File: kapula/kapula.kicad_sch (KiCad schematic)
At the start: 153 parts, among them J1 Conn_02x10_Odd_Even, J12 U.FL, J13 U.FL, J4 Conn_ARM_JTAG_SWD_10, J5 U.FL, J9 U.FL, Q1 AO3401A, Q1 BSS84, Q2 AO3401A, Q3 AO3400A, Q5 AO3400A, Q6 AO3400A, T1 BW21S7511A01TF, T2 BW21S7511A01TF, T3 BW21S7511A01TF, T4 BW21S7511A01TF, U1 XC6206P332MR, U2 TP4054, U3 DW01+G, U5 EFR32FG14P233F256GM48-B, U6 XA213-G4J, X1 DSB221SDN, Y1 32768 Hz

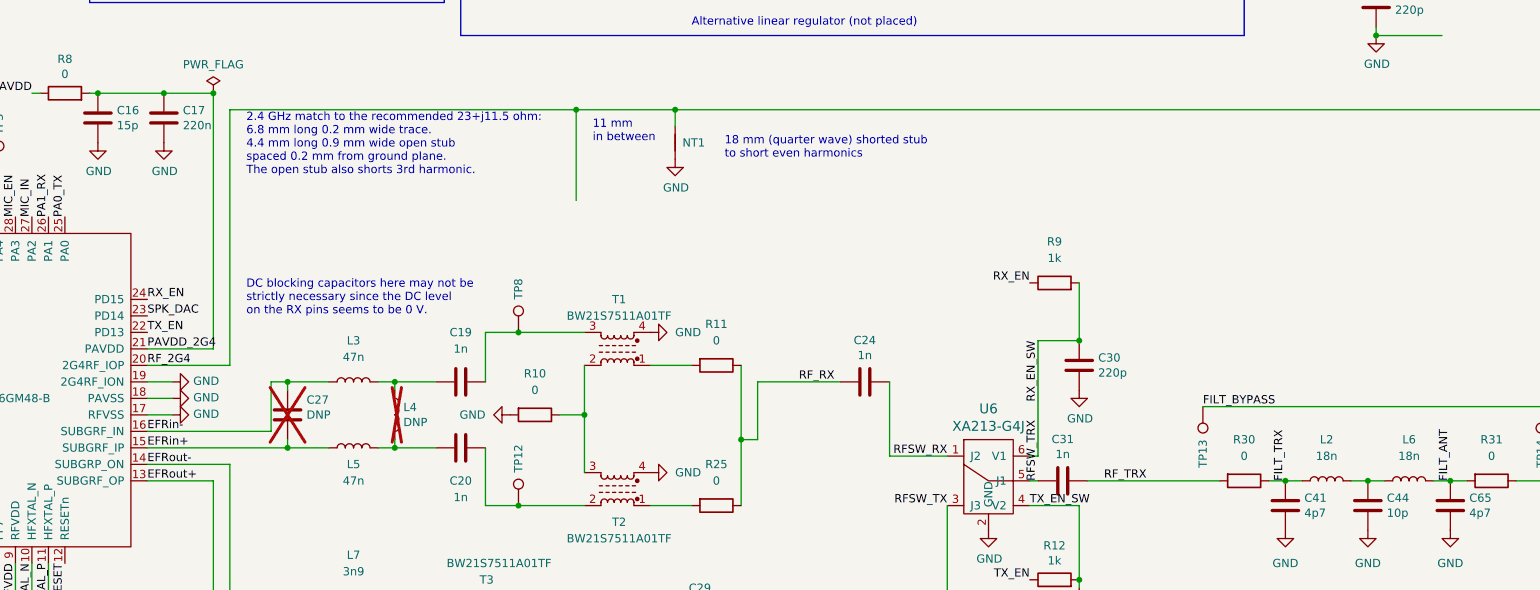
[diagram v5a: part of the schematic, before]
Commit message: PCB: Layout more RF circuits
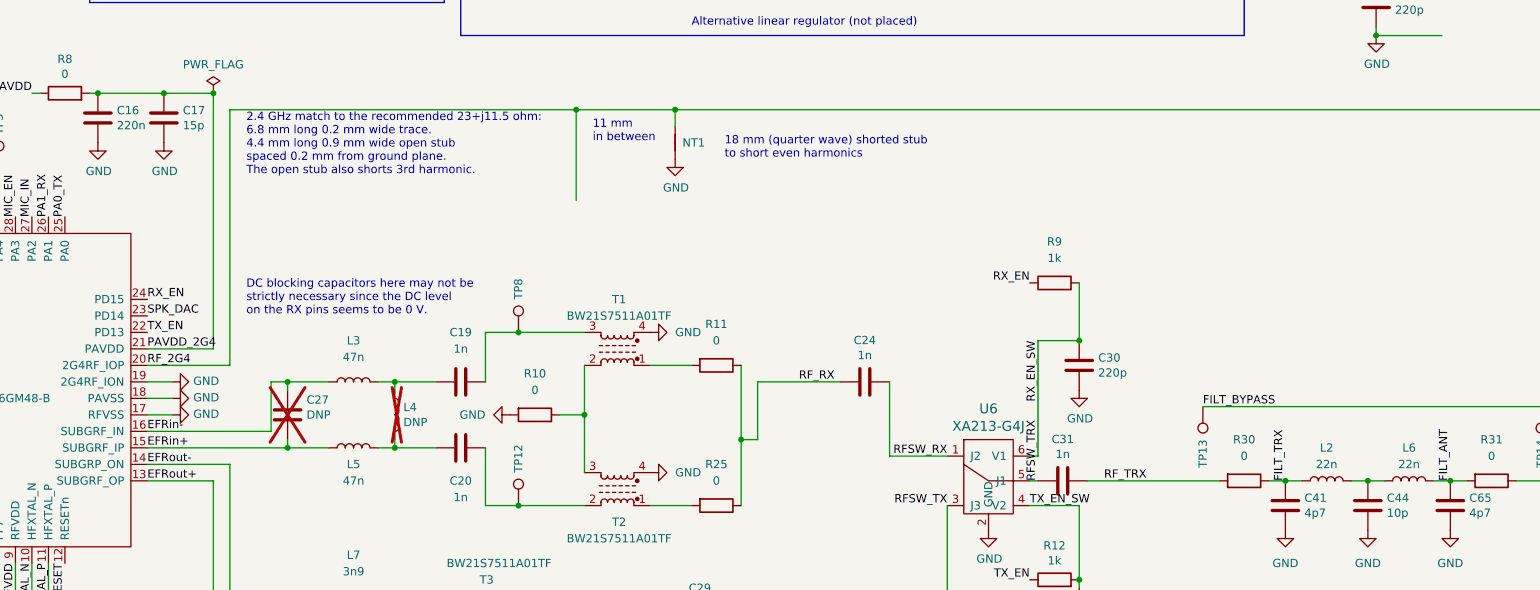
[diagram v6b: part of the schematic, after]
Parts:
- C16: value 15p -> 220n; LCSC C1548 -> C16772
- C17: value 220n -> 15p; LCSC C16772 -> C1548
- C41, C65: LCSC (none) -> C1569
- C44: LCSC (none) -> C32949
- L2, L6: value 18n -> 22n; footprint Inductor_SMD:L_0603_1608Metric_Pad1.05x0.95mm_HandSolder -> kapula:L_0402_to_0603_HandSolder; LCSC (none) -> C12099
- R38, R8: footprint kapula:R_0402_to_0603_HandSolder -> Resistor_SMD:R_0402_1005Metric
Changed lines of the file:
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@@
       (effects (font (size 1.27 1.27)) (justify left))
     )
-    (property "Value" "15p" (at 159.131 87.503 0)
+    (property "Value" "220n" (at 159.131 87.503 0)
       (effects (font (size 1.27 1.27)) (justify left))
     )
@@
       (effects (font (size 1.27 1.27)) hide)
     )
-    (property "LCSC" "C1548" (at 156.21 86.36 0)
+    (property "LCSC" "C16772" (at 156.21 86.36 0)
       (effects (font (size 1.27 1.27)) hide)
     )
@@
       (effects (font (size 1.27 1.27)) (justify left))
     )
-    (property "Value" "220n" (at 169.291 87.503 0)
+    (property "Value" "15p" (at 169.291 87.503 0)
       (effects (font (size 1.27 1.27)) (justify left))
     )
@@
       (effects (font (size 1.27 1.27)) hide)
     )
-    (property "LCSC" "C16772" (at 166.37 86.36 0)
+    (property "LCSC" "C1548" (at 166.37 86.36 0)
       (effects (font (size 1.27 1.27)) hide)
     )
@@
       (effects (font (size 1.27 1.27)))
     )
-    (property "Footprint" "kapula:R_0402_to_0603_HandSolder" (at 151.13 84.328 90)
+    (property "Footprint" "Resistor_SMD:R_0402_1005Metric" (at 151.13 84.328 90)
       (effects (font (size 1.27 1.27)) hide)
     )
@@
       (effects (font (size 1.27 1.27)))
     )
-    (property "Footprint" "kapula:R_0402_to_0603_HandSolder" (at 193.04 191.008 90)
+    (property "Footprint" "Resistor_SMD:R_0402_1005Metric" (at 193.04 191.008 90)
       (effects (font (size 1.27 1.27)) hide)
     )
@@
       (effects (font (size 1.27 1.27)) hide)
     )
-    (property "LCSC" "" (at 351.79 146.05 0)
+    (property "LCSC" "C32949" (at 351.79 146.05 0)
       (effects (font (size 1.27 1.27)) hide)
     )
@@
   (symbol (lib_id "Device:L") (at 358.14 142.24 90) (unit 1)
     (in_bom yes) (on_board yes) (dnp no) (fields_autoplaced)
-    (property "Reference" "L6" (at 358.14 135.89 90)
+    (property "Reference" "L6" (at 358.14 137.16 90)
       (effects (font (size 1.27 1.27)))
     )
-    (property "Value" "18n" (at 358.14 138.43 90)
+    (property "Value" "22n" (at 358.14 139.7 90)
       (effects (font (size 1.27 1.27)))
     )
-    (property "Footprint" "Inductor_SMD:L_0603_1608Metric_Pad1.05x0.95mm_HandSolder" (at 358.14 142.24 0)
+    (property "Footprint" "kapula:L_0402_to_0603_HandSolder" (at 358.14 142.24 0)
       (effects (font (size 1.27 1.27)) hide)
     )
@@
       (effects (font (size 1.27 1.27)) hide)
     )
-    (property "LCSC" "" (at 358.14 142.24 0)
+    (property "LCSC" "C12099" (at 358.14 142.24 0)
       (effects (font (size 1.27 1.27)) hide)
     )
@@
       (effects (font (size 1.27 1.27)) hide)
     )
-    (property "LCSC" "" (at 364.49 146.05 0)
+    (property "LCSC" "C1569" (at 364.49 146.05 0)
       (effects (font (size 1.27 1.27)) hide)
     )
@@
   (symbol (lib_id "Device:L") (at 345.44 142.24 90) (unit 1)
     (in_bom yes) (on_board yes) (dnp no) (fields_autoplaced)
-    (property "Reference" "L2" (at 345.44 135.89 90)
+    (property "Reference" "L2" (at 345.44 137.16 90)
       (effects (font (size 1.27 1.27)))
     )
-    (property "Value" "18n" (at 345.44 138.43 90)
+    (property "Value" "22n" (at 345.44 139.7 90)
       (effects (font (size 1.27 1.27)))
     )
-    (property "Footprint" "Inductor_SMD:L_0603_1608Metric_Pad1.05x0.95mm_HandSolder" (at 345.44 142.24 0)
+    (property "Footprint" "kapula:L_0402_to_0603_HandSolder" (at 345.44 142.24 0)
       (effects (font (size 1.27 1.27)) hide)
     )
@@
       (effects (font (size 1.27 1.27)) hide)
     )
-    (property "LCSC" "" (at 345.44 142.24 0)
+    (property "LCSC" "C12099" (at 345.44 142.24 0)
       (effects (font (size 1.27 1.27)) hide)
     )
@@
       (effects (font (size 1.27 1.27)) hide)
     )
-    (property "LCSC" "" (at 339.09 146.05 0)
+    (property "LCSC" "C1569" (at 339.09 146.05 0)
       (effects (font (size 1.27 1.27)) hide)
     )

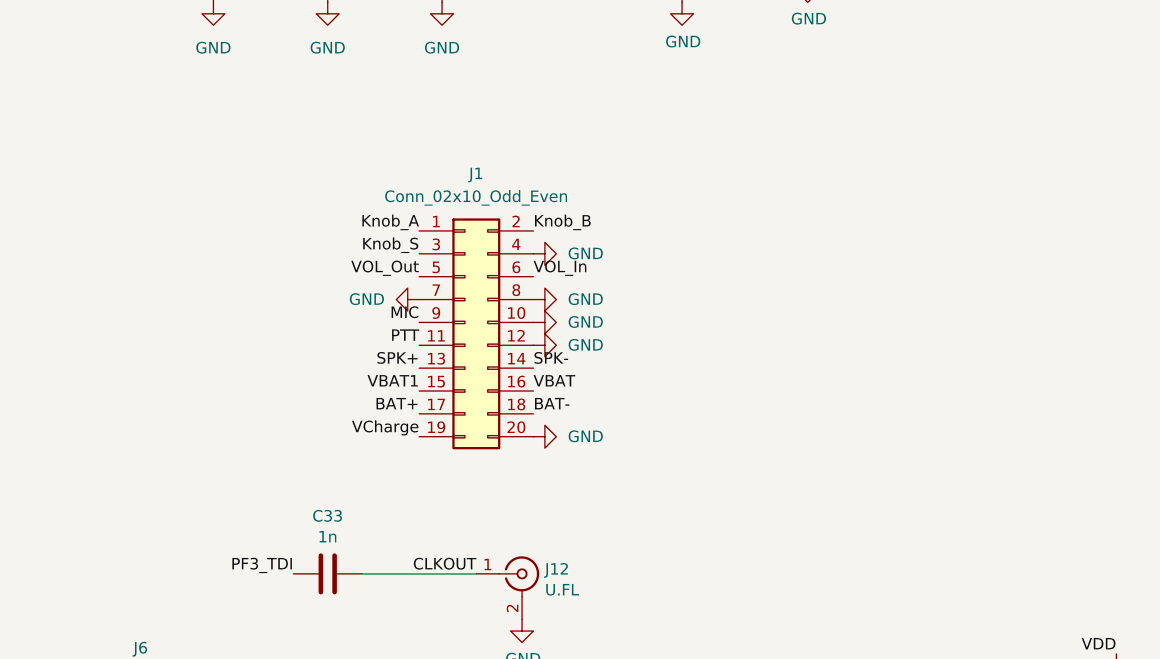
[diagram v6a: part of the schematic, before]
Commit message: PCB: Move components to make space for expansion header
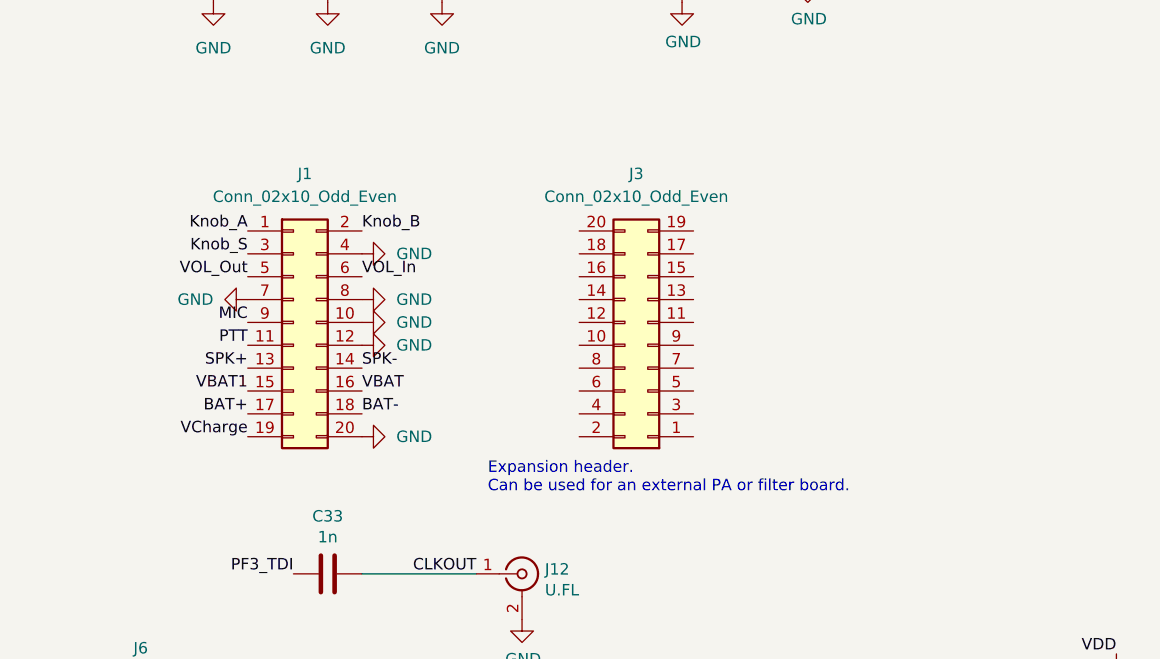
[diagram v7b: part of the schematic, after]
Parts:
- added J3: Conn_02x10_Odd_Even, Connector_PinHeader_2.54mm:PinHeader_2x10_P2.54mm_Vertical, symbol Connector_Generic:Conn_02x10_Odd_Even
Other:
- note added: "Expansion header. Can be used for an external PA or filter board."
- moved on the sheet: J1

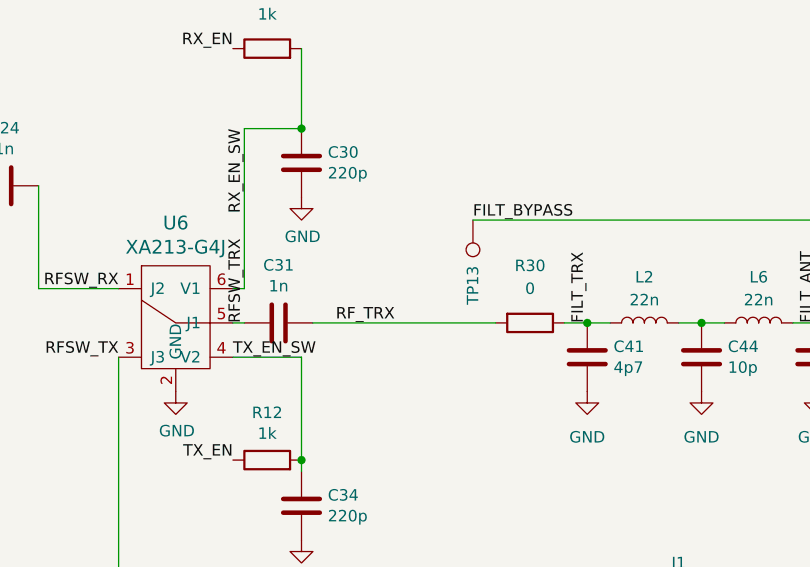
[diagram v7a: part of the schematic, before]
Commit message: PCB: Organize lowpass components to fit them on board again
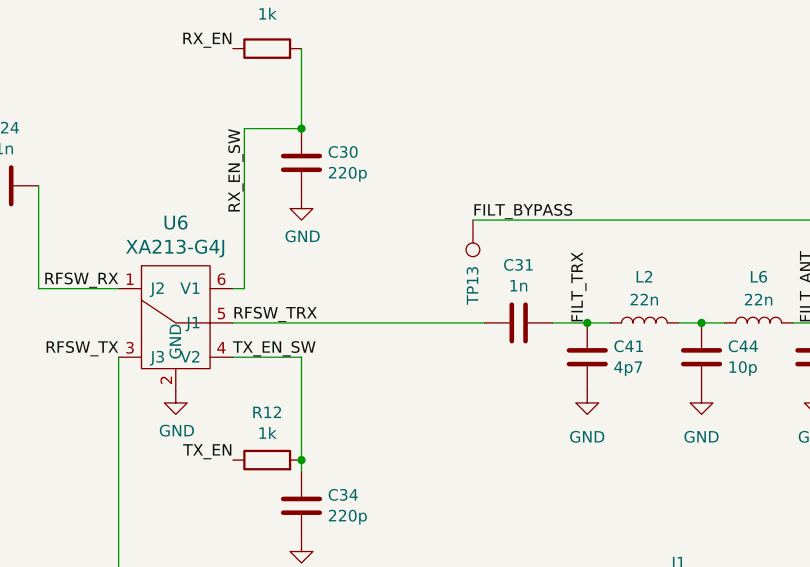
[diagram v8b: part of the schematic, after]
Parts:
- removed R30: 0, kapula:R_0402_to_0603_HandSolder, symbol Device:R
- C31: footprint Capacitor_SMD:C_0402_1005Metric -> kapula:C_0402_to_0603_HandSolder
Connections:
- net RF_TRX is gone; now on net FILT_TRX: C31.1
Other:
- moved on the sheet: C31
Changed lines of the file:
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@@
     (stroke (width 0) (type default))
   )
+  (wire (pts (xy 299.72 142.24) (xy 327.66 142.24))
+    (stroke (width 0) (type default))
+  )
   (wire (pts (xy 307.34 146.05) (xy 299.72 146.05))
     (stroke (width 0) (type default))
@@
     (stroke (width 0) (type default))
   )
-  (wire (pts (xy 308.61 142.24) (xy 328.93 142.24))
-    (stroke (width 0) (type default))
-  )
   (wire (pts (xy 148.59 165.1) (xy 148.59 154.94))
     (stroke (width 0) (type default))
@@
     (stroke (width 0) (type default))
   )
-  (wire (pts (xy 300.99 142.24) (xy 299.72 142.24))
-    (stroke (width 0) (type default))
-  )
-  (wire (pts (xy 336.55 142.24) (xy 339.09 142.24))
+  (wire (pts (xy 335.28 142.24) (xy 339.09 142.24))
     (stroke (width 0) (type default))
   )
@@
     (effects (font (size 1.27 1.27)) (justify right bottom))
   )
-  (label "RFSW_TRX" (at 300.99 142.24 90) (fields_autoplaced)
+  (label "RFSW_TRX" (at 299.72 142.24 0) (fields_autoplaced)
     (effects (font (size 1.27 1.27)) (justify left bottom))
   )
@@
     (effects (font (size 1.27 1.27)) (justify left bottom))
   )
-  (label "RF_TRX" (at 311.15 142.24 0) (fields_autoplaced)
-    (effects (font (size 1.27 1.27)) (justify left bottom))
-  )
   (label "TX_EN" (at 299.72 157.48 180) (fields_autoplaced)
     (effects (font (size 1.27 1.27)) (justify right bottom))
@@
     )
   )
-  (symbol (lib_id "Device:C") (at 304.8 142.24 270) (unit 1)
+  (symbol (lib_id "Device:C") (at 331.47 142.24 270) (unit 1)
     (in_bom yes) (on_board yes) (dnp no)
-    (property "Reference" "C31" (at 304.8 135.8392 90)
+    (property "Reference" "C31" (at 331.47 135.8392 90)
       (effects (font (size 1.27 1.27)))
     )
-    (property "Value" "1n" (at 304.8 138.1506 90)
+    (property "Value" "1n" (at 331.47 138.1506 90)
       (effects (font (size 1.27 1.27)))
     )
-    (property "Footprint" "Capacitor_SMD:C_0402_1005Metric" (at 300.99 143.2052 0)
+    (property "Footprint" "kapula:C_0402_to_0603_HandSolder" (at 327.66 143.2052 0)
       (effects (font (size 1.27 1.27)) hide)
     )
-    (property "Datasheet" "" (at 304.8 142.24 0)
+    (property "Datasheet" "" (at 331.47 142.24 0)
       (effects (font (size 1.27 1.27)) hide)
     )
-    (property "LCSC" "C1523" (at 304.8 142.24 0)
+    (property "LCSC" "C1523" (at 331.47 142.24 0)
       (effects (font (size 1.27 1.27)) hide)
     )
@@
         )
       )
-    )
-  )
-  (symbol (lib_id "Device:R") (at 332.74 142.24 270) (unit 1)
-    (in_bom yes) (on_board yes) (dnp no) (fields_autoplaced)
-    (property "Reference" "R30" (at 332.74 135.89 90)
-      (effects (font (size 1.27 1.27)))
-    )
-    (property "Value" "0" (at 332.74 138.43 90)
-      (effects (font (size 1.27 1.27)))
-    )
-    (property "Footprint" "kapula:R_0402_to_0603_HandSolder" (at 332.74 140.462 90)
-      (effects (font (size 1.27 1.27)) hide)
-    )
-    (property "Datasheet" "" (at 332.74 142.24 0)
-      (effects (font (size 1.27 1.27)) hide)
-    )
-    (property "LCSC" "C17168" (at 332.74 142.24 0)
-      (effects (font (size 1.27 1.27)) hide)
-    )
-    (pin "1")
-    (pin "2")
-    (instances
-      (project "kapula"
-        (path "/f2315993-072e-45c9-8c85-e79c6d40aba4"
-          (reference "R30") (unit 1)
-        )
-      )
